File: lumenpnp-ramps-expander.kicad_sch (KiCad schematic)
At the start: 70 parts, among them J1 12/24V, J10 A_MICROSTEPS, J11 A_DIAG, J12 A_VDD, J13 DIAG, J14 B_MICROSTEPS, J15 A_DIAG, J16 B_VDD, J2 EXP1, J3 EXP2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

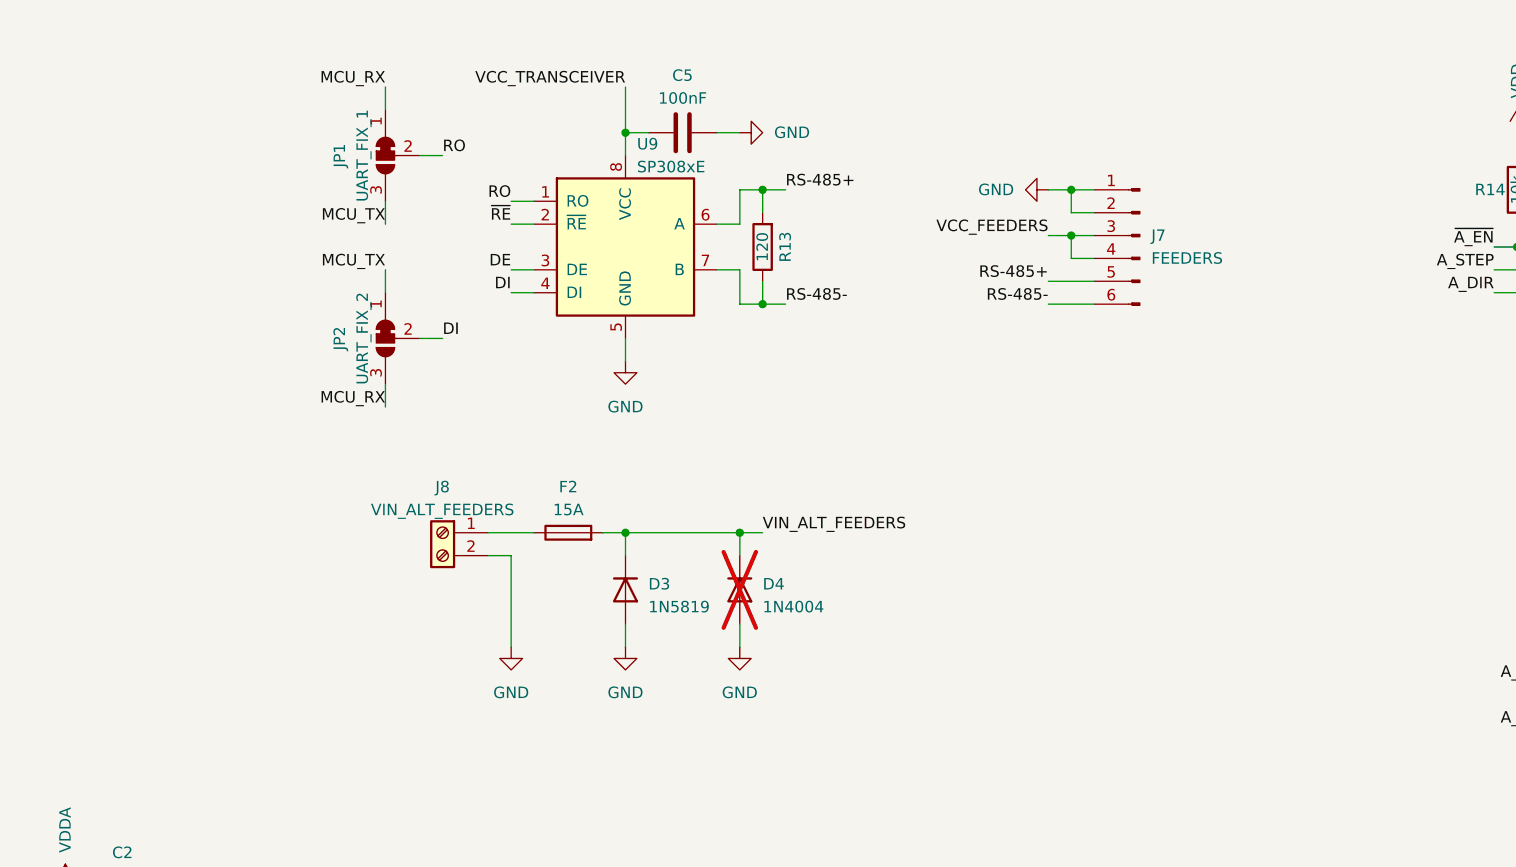
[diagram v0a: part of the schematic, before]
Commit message: Add NIS4461 efuse for feeder power
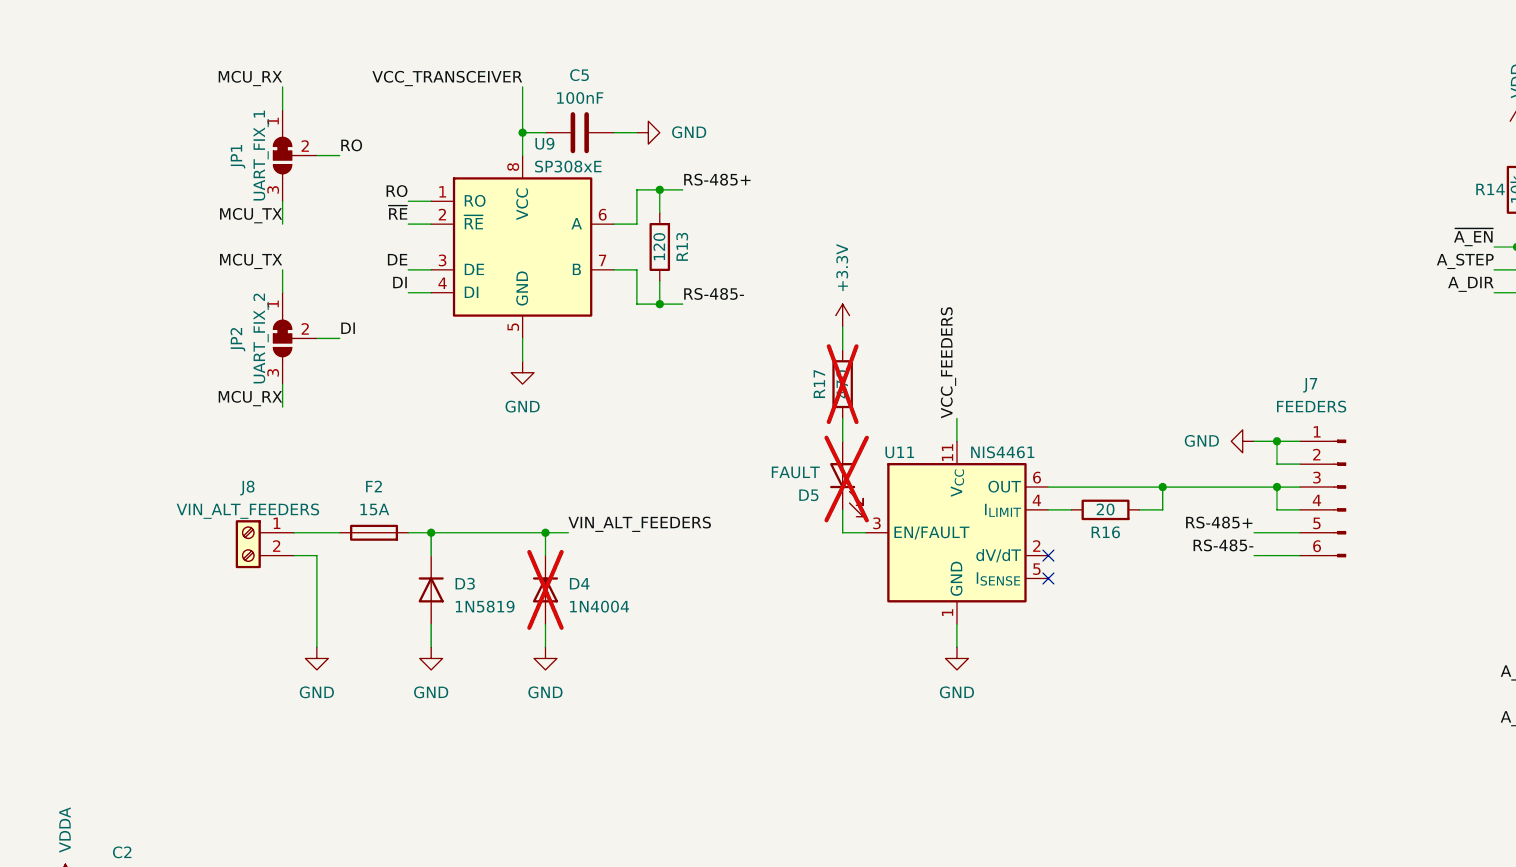
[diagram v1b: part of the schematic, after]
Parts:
- added D5: FAULT, LED_SMD:LED_0603_1608Metric, symbol Device:LED
- added R16: 20, Resistor_SMD:R_0603_1608Metric, symbol Device:R
- added R17: 470, Resistor_SMD:R_0603_1608Metric, symbol Device:R
- added U11: NIS4461, Package_DFN_QFN:WDFN-10-1EP_3x3mm_P0.5mm_EP1.8x2.5mm, symbol expander:NIS4461
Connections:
- net +3.3V: now also R17.2
- net GND: now also U11.1 (GND)
- net VCC_FEEDERS: now also U11.11 (V_{CC}); no longer J7.3 (Pin_3), J7.4 (Pin_4)
- new net: J7.3 (Pin_3), J7.4 (Pin_4), R16.2, U11.10 (OUT), U11.6 (OUT), U11.7 (OUT), U11.8 (OUT), U11.9 (OUT)
- new net: D5.1 (K), U11.3 (EN/FAULT)
- new net: R16.1, U11.4 (I_{LIMIT})
- new net: D5.2 (A), R17.1
- no-connect marks 6 -> 8
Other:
- moved on the sheet: C5, D3, D4, F2, J7, J8, JP1, JP2, R13, U9
